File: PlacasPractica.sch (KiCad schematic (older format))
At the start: 66 parts, among them J1 USB_OTG, J2 Conn_01x10, J3 Conn_01x10, J4 CONN_02X05, SW1 SW_Push, U1 SAMD20J18A-AU, U2 XBEE, U3 MB85RC64VPNF-G-JNERE1, U4 XC6220B331MR-G, U5 XC6220B331MR-G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

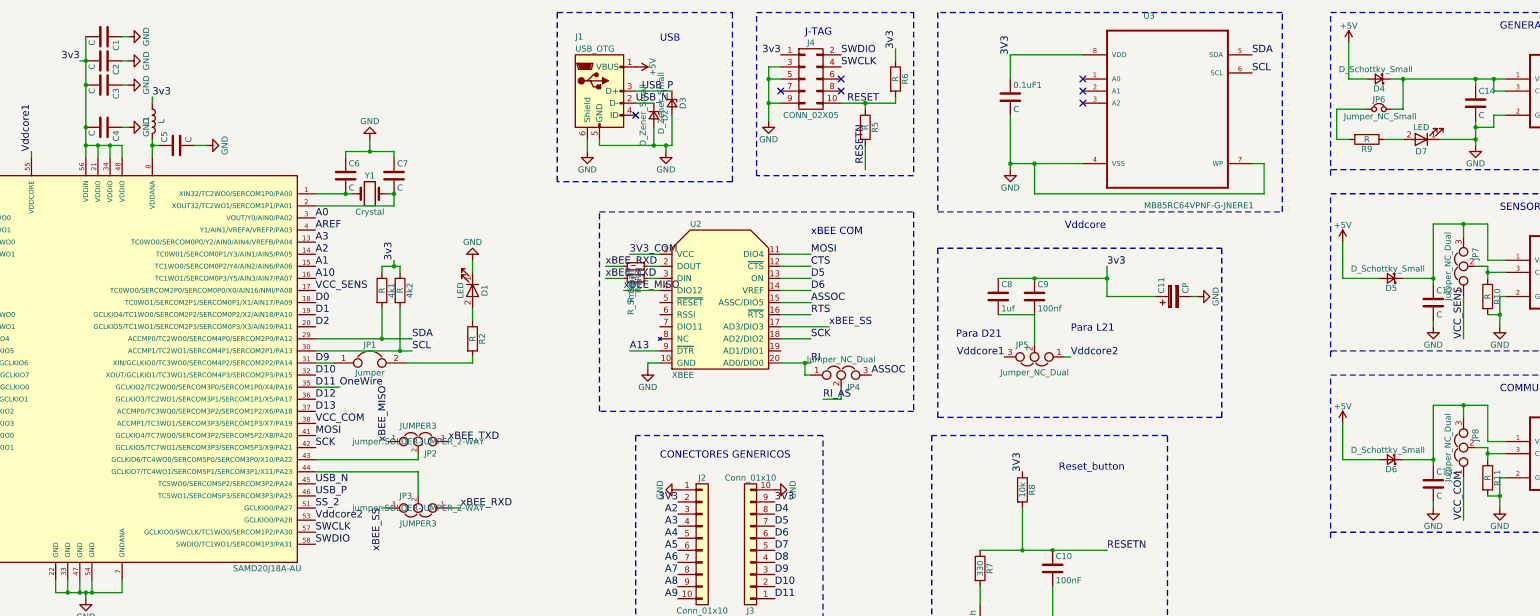
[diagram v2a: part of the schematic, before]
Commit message: Agujeros de montaje y seriagrafía añadidos
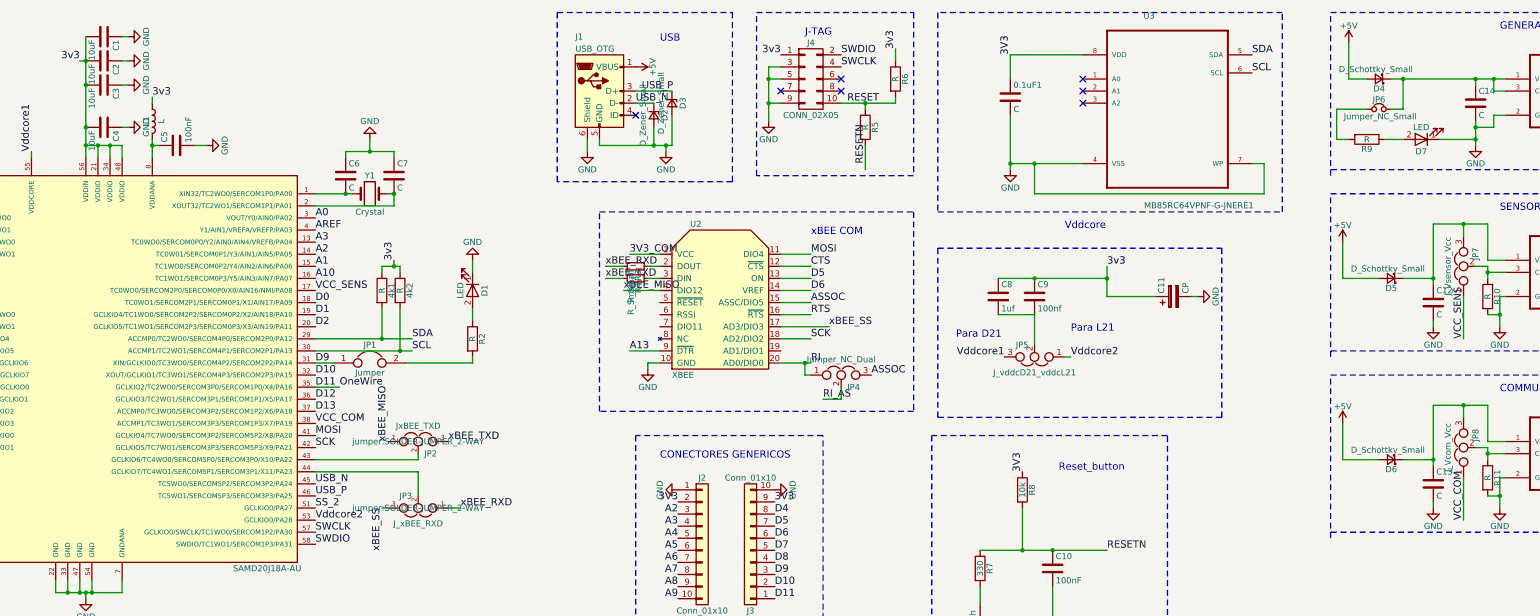
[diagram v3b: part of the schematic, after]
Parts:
- C1, C2, C3, C4: value C -> 10uF
- C5: value C -> 100nF
- JP2: value JUMPER3 -> JxBEE_TXD
- JP3: value JUMPER3 -> J_xBEE_RXD
- JP5: value Jumper_NC_Dual -> J_vddcD21_vddcL21
- JP7: value Jumper_NC_Dual -> J_Vsensor_Vcc
- JP8: value Jumper_NC_Dual -> J_Vcom_Vcc
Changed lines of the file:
@@
 P 2650 1550
 F 0 "C4" H 2675 1650 50  0000 L CNN
-F 1 "C" H 2675 1450 50  0000 L CNN
+F 1 "10uF" H 2675 1450 50  0000 L CNN
 F 2 "Capacitors_SMD:C_0805_HandSoldering" H 2688 1400 50  0001 C CNN
 F 3 "" H 2650 1550 50  0001 C CNN
@@
 P 2650 1200
 F 0 "C3" H 2675 1300 50  0000 L CNN
-F 1 "C" H 2675 1100 50  0000 L CNN
+F 1 "10uF" H 2675 1100 50  0000 L CNN
 F 2 "Capacitors_SMD:C_0805_HandSoldering" H 2688 1050 50  0001 C CNN
 F 3 "" H 2650 1200 50  0001 C CNN
@@
 P 2650 1000
 F 0 "C2" H 2675 1100 50  0000 L CNN
-F 1 "C" H 2675 900 50  0000 L CNN
+F 1 "10uF" H 2675 900 50  0000 L CNN
 F 2 "Capacitors_SMD:C_0805_HandSoldering" H 2688 850 50  0001 C CNN
 F 3 "" H 2650 1000 50  0001 C CNN
@@
 P 2650 800
 F 0 "C1" H 2675 900 50  0000 L CNN
-F 1 "C" H 2675 700 50  0000 L CNN
+F 1 "10uF" H 2675 700 50  0000 L CNN
 F 2 "Capacitors_SMD:C_0805_HandSoldering" H 2688 650 50  0001 C CNN
 F 3 "" H 2650 800 50  0001 C CNN
@@
 P 3250 1700
 F 0 "C5" H 3275 1800 50  0000 L CNN
-F 1 "C" H 3275 1600 50  0000 L CNN
+F 1 "100nF" H 3275 1600 50  0000 L CNN
 F 2 "Capacitors_SMD:C_0805_HandSoldering" H 3288 1550 50  0001 C CNN
 F 3 "" H 3250 1700 50  0001 C CNN
@@
 P 5250 4150
 F 0 "JP2" H 5300 4050 50  0000 L CNN
-F 1 "JUMPER3" H 5250 4250 50  0000 C BNN
+F 1 "JxBEE_TXD" H 5250 4250 50  0000 C BNN
 F 2 "jumper:SOLDER-JUMPER_2-WAY" H 5250 4150 50  0000 C CNN
 F 3 "" H 5250 4150 50  0000 C CNN
@@
 P 5250 4700
 F 0 "JP3" H 5300 4600 50  0000 L CNN
-F 1 "JUMPER3" H 5250 4800 50  0000 C BNN
+F 1 "J_xBEE_RXD" H 5250 4800 50  0000 C BNN
 F 2 "jumper:SOLDER-JUMPER_2-WAY" H 5250 4700 50  0000 C CNN
 F 3 "" H 5250 4700 50  0000 C CNN
@@
 P 13900 2700
 F 0 "JP7" H 13950 2600 50  0000 L CNN
-F 1 "Jumper_NC_Dual" H 13900 2800 50  0000 C BNN
+F 1 "J_Vsensor_Vcc" H 13900 2800 50  0000 C BNN
 F 2 "jumper:SOLDER-JUMPER_2-WAY" H 13900 2700 50  0001 C CNN
 F 3 "" H 13900 2700 50  0001 C CNN
@@
 P 13900 4200
 F 0 "JP8" H 13950 4100 50  0000 L CNN
-F 1 "Jumper_NC_Dual" H 13900 4300 50  0000 C BNN
+F 1 "J_Vcom_Vcc" H 13900 4300 50  0000 C BNN
 F 2 "jumper:SOLDER-JUMPER_2-WAY" H 13900 4200 50  0001 C CNN
 F 3 "" H 13900 4200 50  0001 C CNN
@@
 P 10350 3450
 F 0 "JP5" H 10400 3350 50  0000 L CNN
-F 1 "Jumper_NC_Dual" H 10350 3550 50  0000 C BNN
+F 1 "J_vddcD21_vddcL21" H 10350 3550 50  0000 C BNN
 F 2 "jumper:SOLDER-JUMPER_2-WAY" H 10350 3450 50  0001 C CNN
 F 3 "" H 10350 3450 50  0001 C CNN

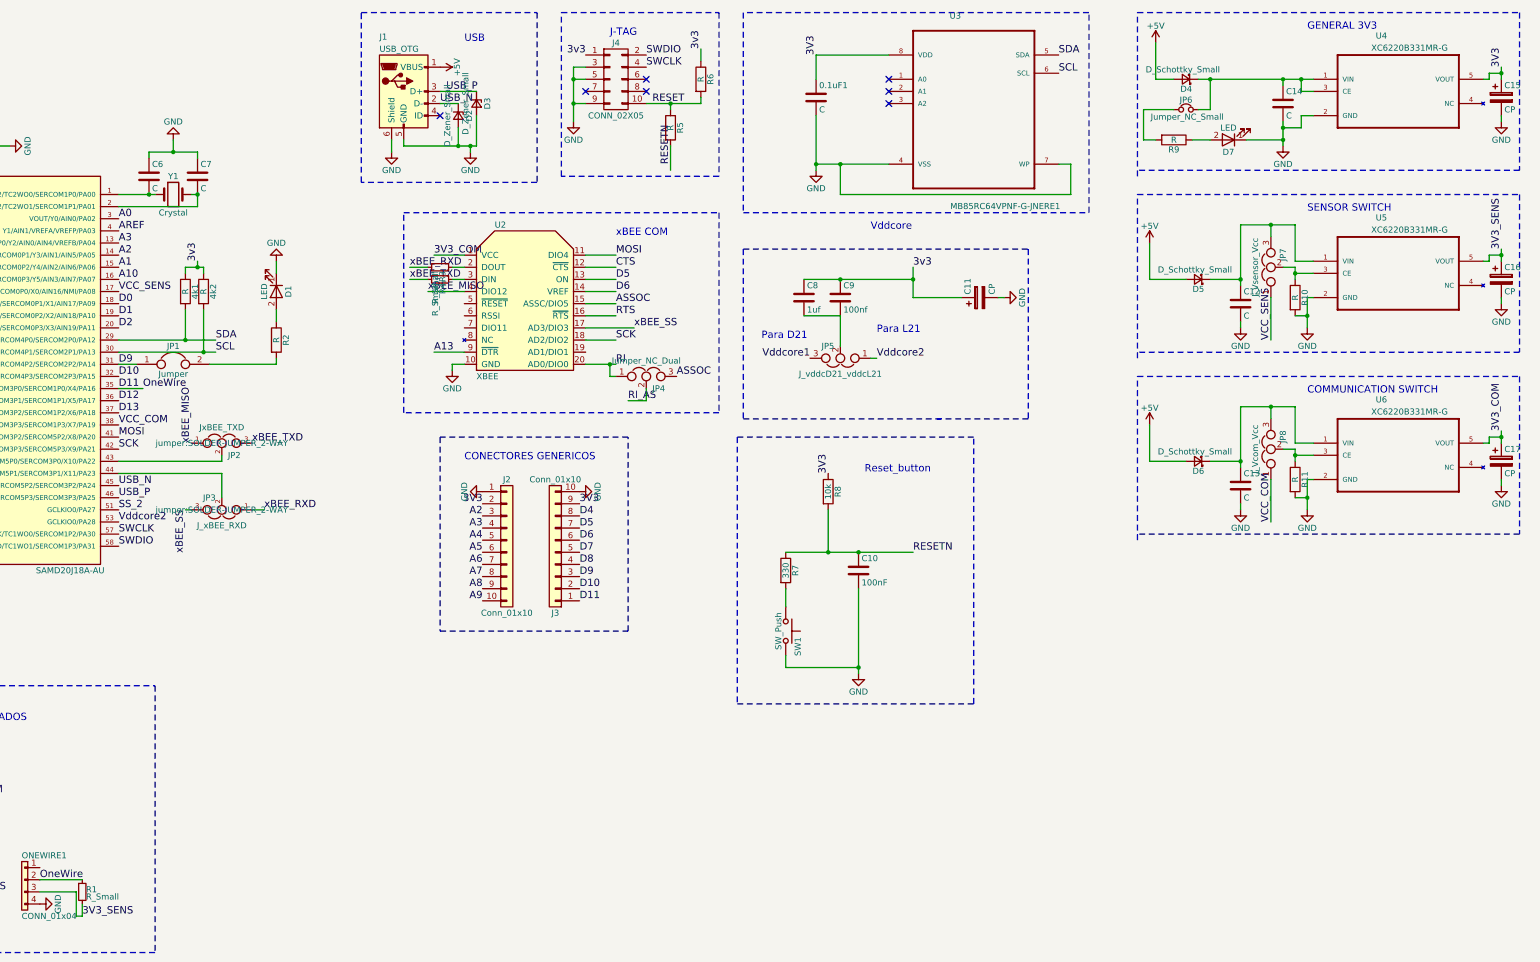
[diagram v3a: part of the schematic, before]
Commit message: Lista de materiales añadida.
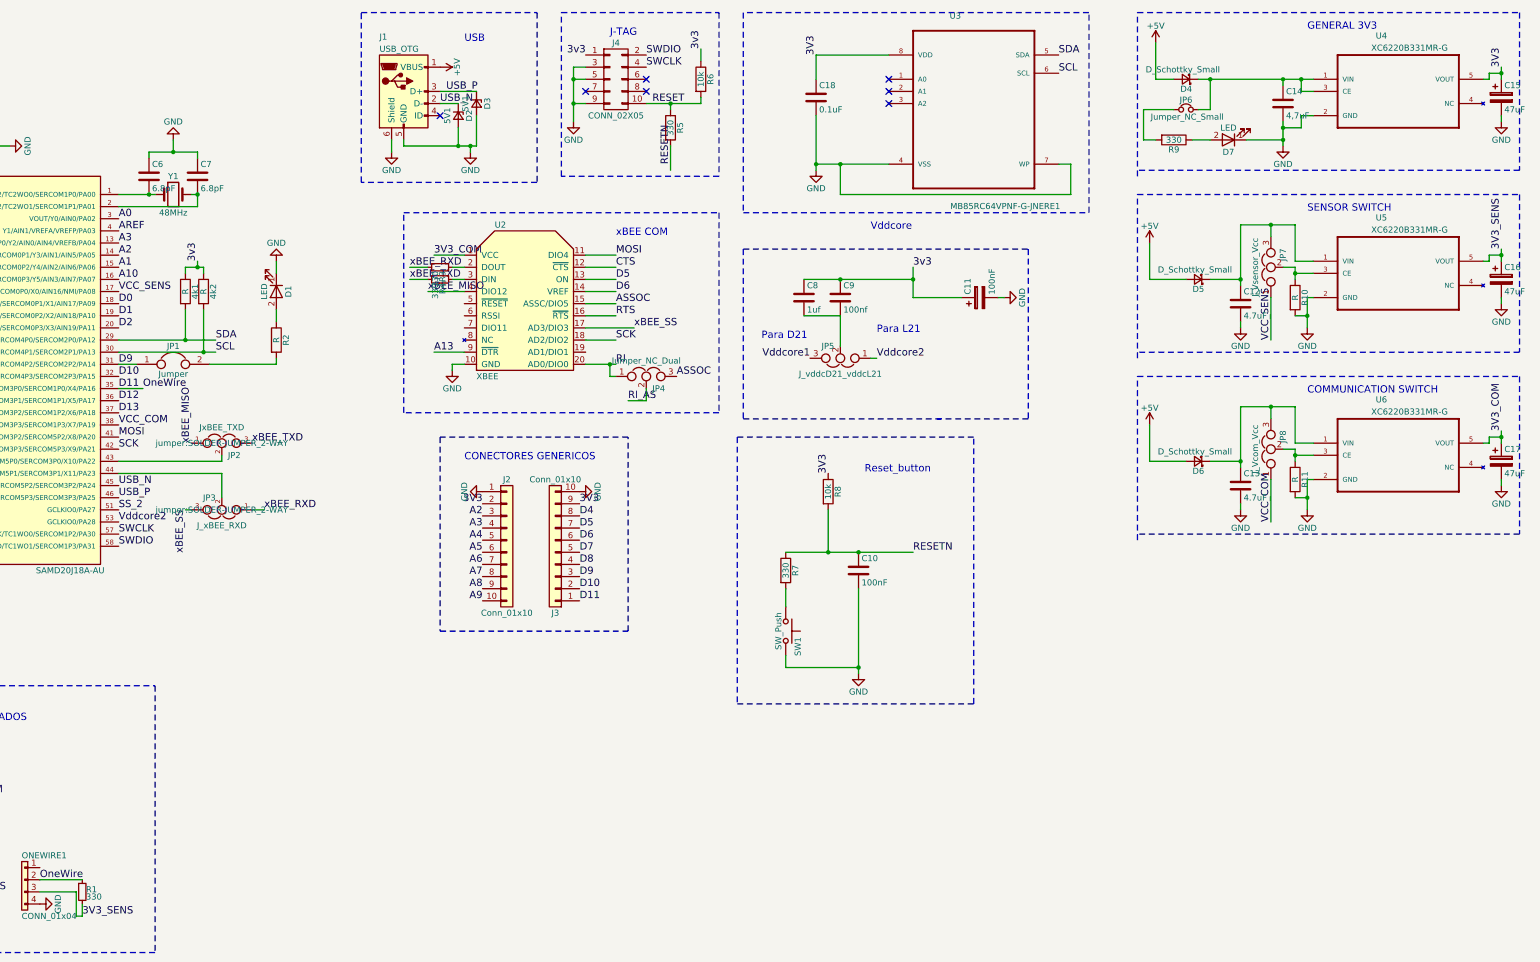
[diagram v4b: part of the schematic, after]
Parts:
- C11: value CP -> 100nF
- C12, C13: value C -> 4.7uF
- C14: value C -> 4,7uF
- C15, C16, C17: value CP -> 47uF
- C18: renamed from 0.1uF1; value C -> 0.1uF
- C6, C7: value C -> 6.8pF
- D2, D3: value D_Zener_Small -> 5V1
- R1, R3, R4: value R_Small -> 330
- R5, R9: value R -> 330
- R6: value R -> 10k
- Y1: value Crystal -> 48MHz
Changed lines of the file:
@@
 P 4100 7850
 F 0 "R1" H 4130 7870 50  0000 L CNN
-F 1 "R_Small" H 4130 7810 50  0000 L CNN
+F 1 "330" H 4130 7810 50  0000 L CNN
 F 2 "Resistors_SMD:R_0805_HandSoldering" H 4100 7850 50  0001 C CNN
 F 3 "" H 4100 7850 50  0001 C CNN
@@
 P 11500 2950
 F 0 "C11" H 11525 3050 50  0000 L CNN
-F 1 "CP" H 11525 2850 50  0000 L CNN
+F 1 "100nF" H 11525 2850 50  0000 L CNN
 F 2 "Capacitors_SMD:CP_Elec_6.3x5.8" H 11538 2800 50  0001 C CNN
 F 3 "" H 11500 2950 50  0001 C CNN
@@
 P 4650 1950
 F 0 "C6" H 4675 2050 50  0000 L CNN
-F 1 "C" H 4675 1850 50  0000 L CNN
+F 1 "6.8pF" H 4675 1850 50  0000 L CNN
 F 2 "Capacitors_SMD:C_0805_HandSoldering" H 4688 1800 50  0001 C CNN
 F 3 "" H 4650 1950 50  0001 C CNN
@@
 P 5050 1950
 F 0 "C7" H 5075 2050 50  0000 L CNN
-F 1 "C" H 5075 1850 50  0000 L CNN
+F 1 "6.8pF" H 5075 1850 50  0000 L CNN
 F 2 "Capacitors_SMD:C_0805_HandSoldering" H 5088 1800 50  0001 C CNN
 F 3 "" H 5050 1950 50  0001 C CNN
@@
 P 4850 2100
 F 0 "Y1" H 4850 2250 50  0000 C CNN
-F 1 "Crystal" H 4850 1950 50  0000 C CNN
+F 1 "48MHz" H 4850 1950 50  0000 C CNN
 F 2 "Crystals:Crystal_SMD_0603-2pin_6.0x3.5mm_HandSoldering" H 4850 2100 50  0001 C CNN
 F 3 "" H 4850 2100 50  0001 C CNN
@@
 P 13100 1650
 F 0 "R9" V 13180 1650 50  0000 C CNN
-F 1 "R" V 13100 1650 50  0000 C CNN
+F 1 "330" V 13100 1650 50  0000 C CNN
 F 2 "Resistors_SMD:R_0805_HandSoldering" V 13030 1650 50  0001 C CNN
 F 3 "" H 13100 1650 50  0001 C CNN
@@
 P 7200 1450
 F 0 "D2" H 7200 1540 50  0000 C CNN
-F 1 "D_Zener_Small" H 7200 1360 50  0000 C CNN
+F 1 "5V1" H 7200 1360 50  0000 C CNN
 F 2 "Diodes_SMD:D_SOD-323_HandSoldering" V 7200 1450 50  0001 C CNN
 F 3 "" V 7200 1450 50  0001 C CNN
@@
 P 7350 1350
 F 0 "D3" H 7350 1440 50  0000 C CNN
-F 1 "D_Zener_Small" H 7350 1260 50  0000 C CNN
+F 1 "5V1" H 7350 1260 50  0000 C CNN
 F 2 "Diodes_SMD:D_SOD-323_HandSoldering" V 7350 1350 50  0001 C CNN
 F 3 "" V 7350 1350 50  0001 C CNN
@@
 P 9200 1150
 F 0 "R6" V 9280 1150 50  0000 C CNN
-F 1 "R" V 9200 1150 50  0000 C CNN
+F 1 "10k" V 9200 1150 50  0000 C CNN
 F 2 "Resistors_SMD:R_0805_HandSoldering" V 9130 1150 50  0001 C CNN
 F 3 "" H 9200 1150 50  0001 C CNN
@@
 P 8950 1550
 F 0 "R5" V 9030 1550 50  0000 C CNN
-F 1 "R" V 8950 1550 50  0000 C CNN
+F 1 "330" V 8950 1550 50  0000 C CNN
 F 2 "Resistors_SMD:R_0805_HandSoldering" V 8880 1550 50  0001 C CNN
 F 3 "" H 8950 1550 50  0001 C CNN
@@
 P 7050 2700
 F 0 "R3" H 7080 2720 50  0000 L CNN
-F 1 "R_Small" H 7080 2660 50  0000 L CNN
+F 1 "330" H 7080 2660 50  0000 L CNN
 F 2 "Resistors_SMD:R_0805_HandSoldering" H 7050 2700 50  0001 C CNN
 F 3 "" H 7050 2700 50  0001 C CNN
@@
 P 7050 2800
 F 0 "R4" H 7080 2820 50  0000 L CNN
-F 1 "R_Small" H 7080 2760 50  0000 L CNN
+F 1 "330" H 7080 2760 50  0000 L CNN
 F 2 "Resistors_SMD:R_0805_HandSoldering" H 7050 2800 50  0001 C CNN
 F 3 "" H 7050 2800 50  0001 C CNN
@@
 NoConn ~ 8250 1250
 $Comp
-L C 0.1uF1
+L C C18
 U 1 1 5AB3BCB4
 P 10150 1300
-F 0 "0.1uF1" H 10175 1400 50  0000 L CNN
-F 1 "C" H 10175 1200 50  0000 L CNN
+F 0 "C18" H 10175 1400 50  0000 L CNN
+F 1 "0.1uF" H 10175 1200 50  0000 L CNN
 F 2 "Capacitors_SMD:C_0805_HandSoldering" H 10188 1150 50  0001 C CNN
 F 3 "" H 10150 1300 50  0001 C CNN
@@
 P 13650 3000
 F 0 "C12" H 13675 3100 50  0000 L CNN
-F 1 "C" H 13675 2900 50  0000 L CNN
+F 1 "4.7uF" H 13675 2900 50  0000 L CNN
 F 2 "Capacitors_SMD:C_0805_HandSoldering" H 13688 2850 50  0001 C CNN
 F 3 "" H 13650 3000 50  0001 C CNN
@@
 P 15800 2800
 F 0 "C16" H 15825 2900 50  0000 L CNN
-F 1 "CP" H 15825 2700 50  0000 L CNN
+F 1 "47uF" H 15825 2700 50  0000 L CNN
 F 2 "Capacitors_SMD:CP_Elec_6.3x5.8" H 15838 2650 50  0001 C CNN
 F 3 "" H 15800 2800 50  0001 C CNN
@@
 P 14000 1350
 F 0 "C14" H 14025 1450 50  0000 L CNN
-F 1 "C" H 14025 1250 50  0000 L CNN
+F 1 "4,7uF" H 14025 1250 50  0000 L CNN
 F 2 "Capacitors_SMD:C_0805_HandSoldering" H 14038 1200 50  0001 C CNN
 F 3 "" H 14000 1350 50  0001 C CNN
@@
 P 15800 1300
 F 0 "C15" H 15825 1400 50  0000 L CNN
-F 1 "CP" H 15825 1200 50  0000 L CNN
+F 1 "47uF" H 15825 1200 50  0000 L CNN
 F 2 "Capacitors_SMD:CP_Elec_6.3x5.8" H 15838 1150 50  0001 C CNN
 F 3 "" H 15800 1300 50  0001 C CNN
@@
 P 13650 4500
 F 0 "C13" H 13675 4600 50  0000 L CNN
-F 1 "C" H 13675 4400 50  0000 L CNN
+F 1 "4.7uF" H 13675 4400 50  0000 L CNN
 F 2 "Capacitors_SMD:C_0805_HandSoldering" H 13688 4350 50  0001 C CNN
 F 3 "" H 13650 4500 50  0001 C CNN
@@
 P 15800 4300
 F 0 "C17" H 15825 4400 50  0000 L CNN
-F 1 "CP" H 15825 4200 50  0000 L CNN
+F 1 "47uF" H 15825 4200 50  0000 L CNN
 F 2 "Capacitors_SMD:CP_Elec_6.3x5.8" H 15838 4150 50  0001 C CNN
 F 3 "" H 15800 4300 50  0001 C CNN

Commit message: Añadidos chips criptograficos.
Se ha añadido los chips de criptografia.
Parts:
- added U7: 24AA02, TO_SOT_Packages_SMD:SOT-23-5, symbol 24AA02
- added U8: ATSHA204A, Housings_SOIC:SOIC-8_3.9x4.9mm_Pitch1.27mm, symbol ATSHA204A
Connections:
- wire segments 201 -> 203
- no-connect marks 7 -> 11
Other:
- note added: "CRYPTO CHIPS"
